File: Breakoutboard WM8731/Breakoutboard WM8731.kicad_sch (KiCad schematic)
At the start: 42 parts

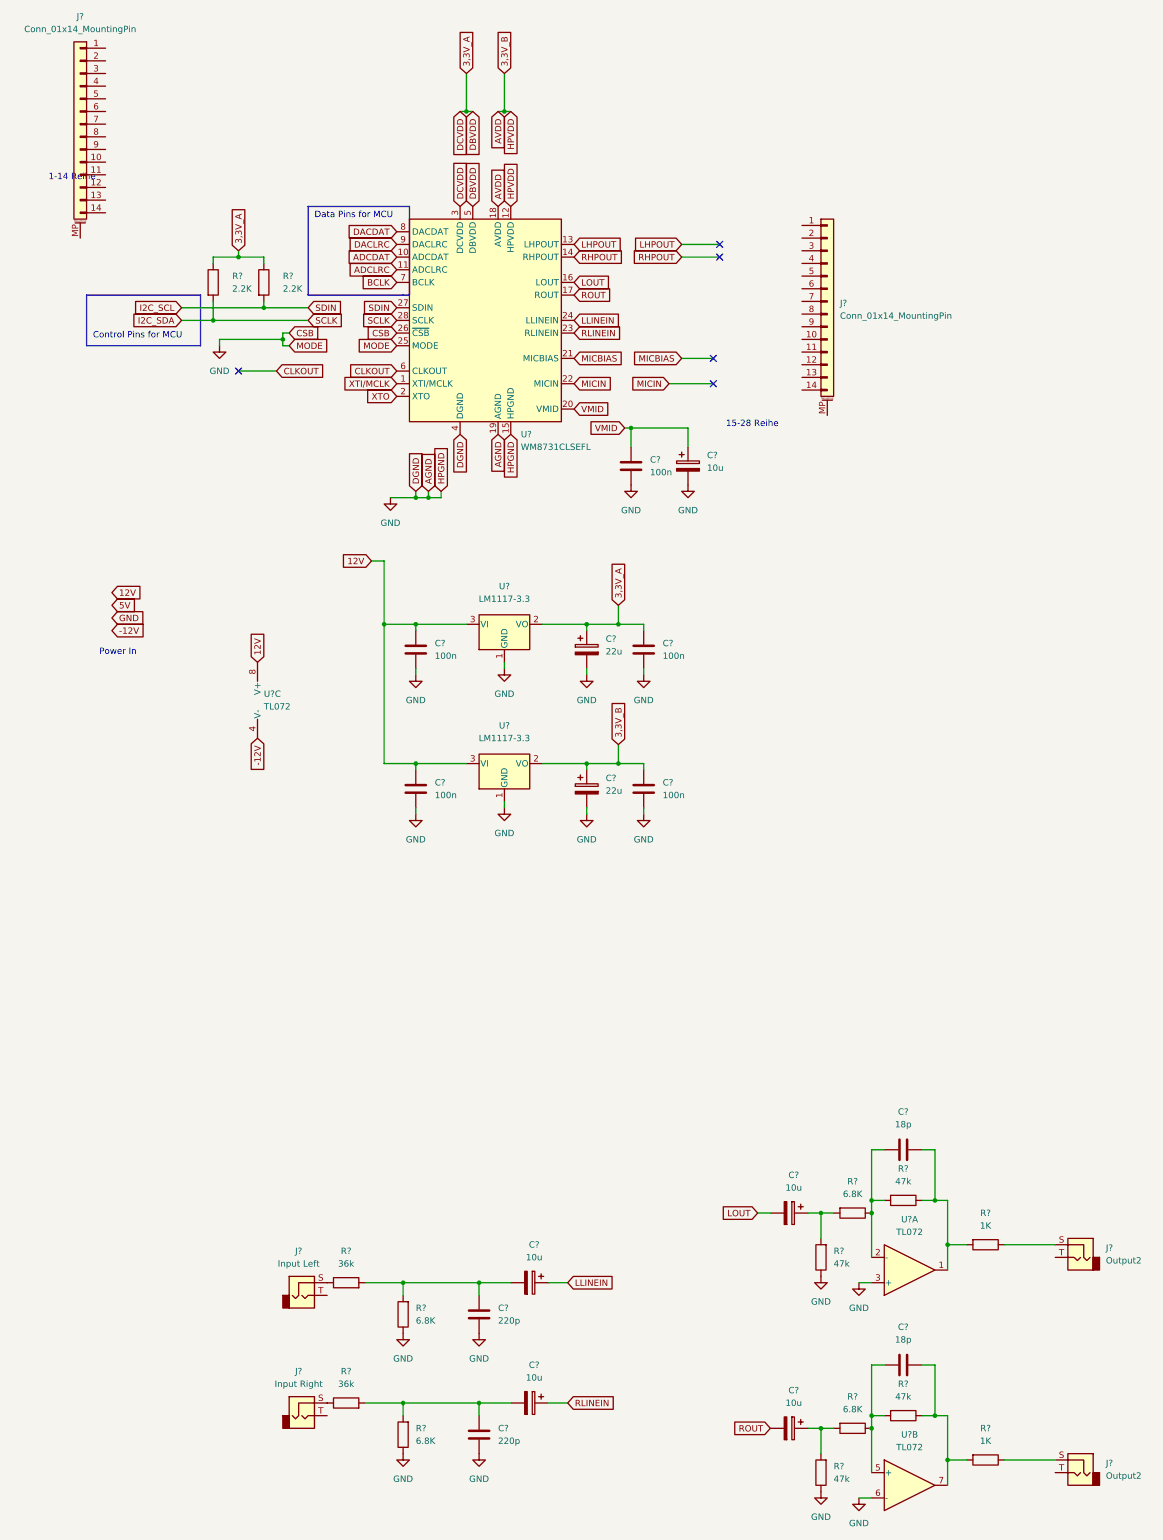
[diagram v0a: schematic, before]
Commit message: added esp sheet
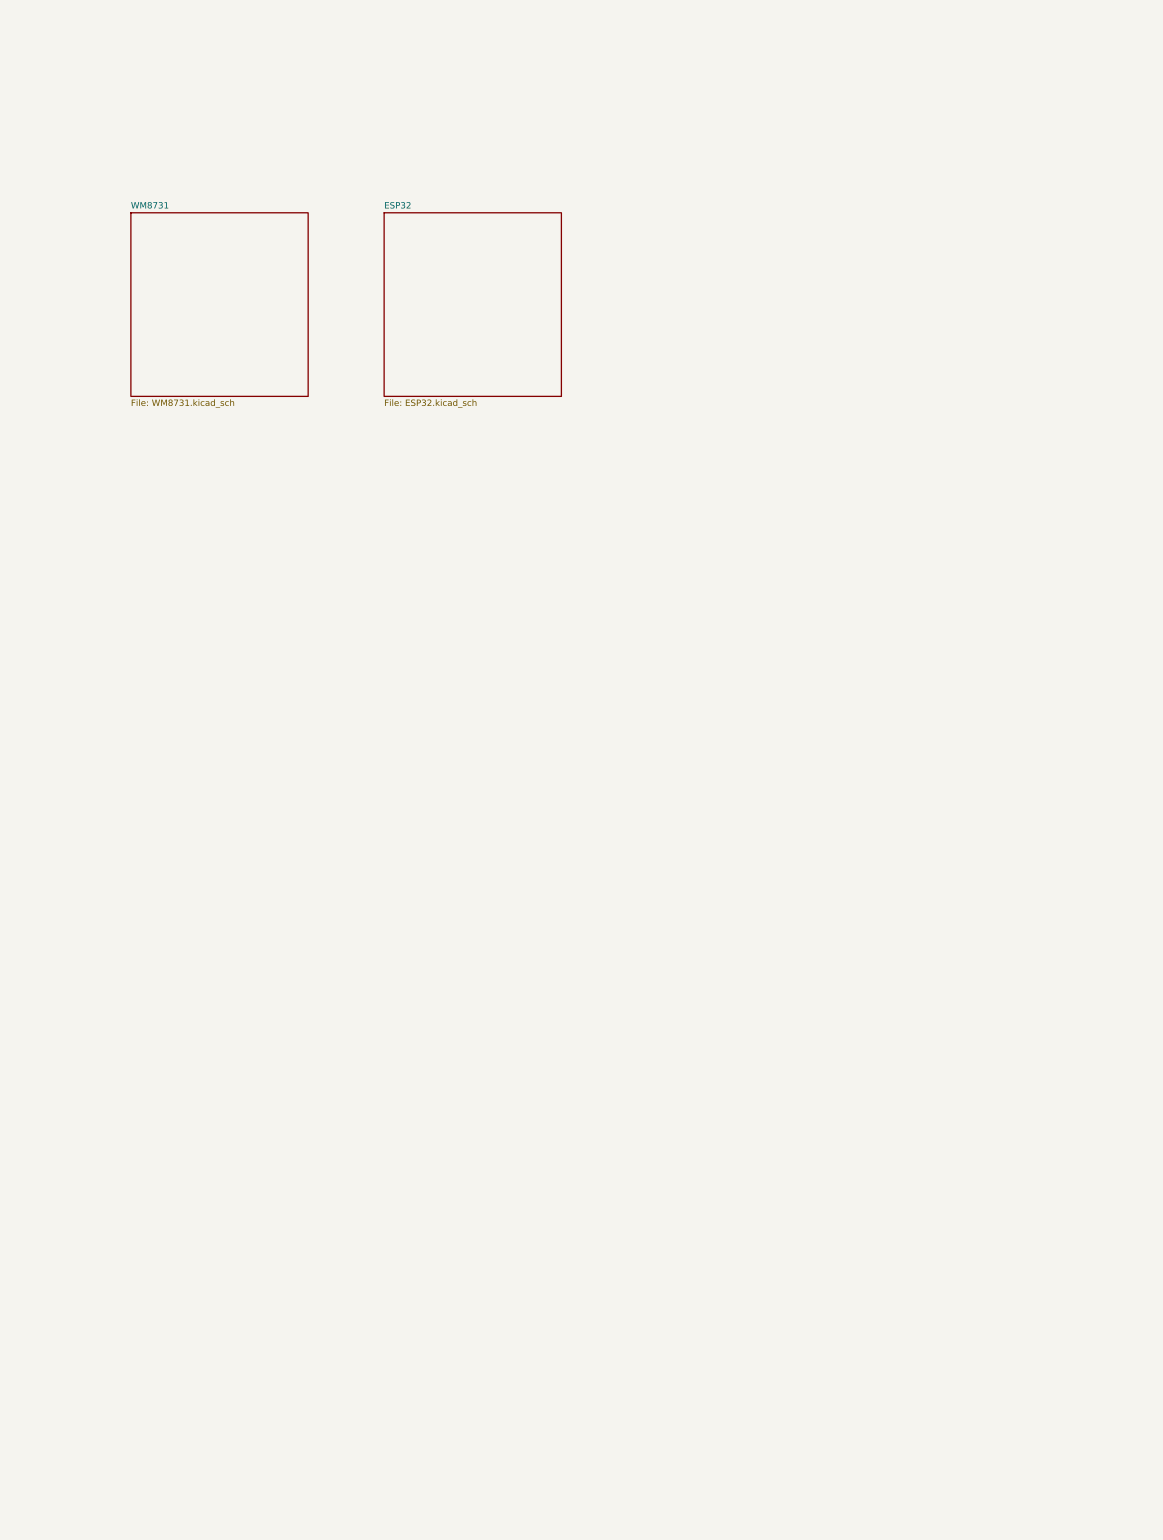
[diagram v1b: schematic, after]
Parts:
- removed C? (x2): 220p, symbol Device:C
- removed C? (x2): 22u, symbol Device:C_Polarized
- removed C? (x5): 10u, symbol Device:C_Polarized
- removed C? (x5): 100n, symbol Device:C
- removed C? (x2): 18p, symbol Device:C
- removed J? (x2): Output2, symbol Connector:AudioJack2
- removed J?: Input Left, symbol Connector:AudioJack2
- removed J? (x2): Conn_01x14_MountingPin, symbol Connector_Generic_MountingPin:Conn_01x14_MountingPin
- removed J?: Input Right, symbol Connector:AudioJack2
- removed R? (x2): 2.2K, symbol Device:R
- removed R? (x4): 6.8K, symbol Device:R
- removed R? (x4): 47k, symbol Device:R
- removed R? (x2): 36k, symbol Device:R
- removed R? (x2): 1K, symbol Device:R
- removed U? (x2): LM1117-3.3, symbol Regulator_Linear:LM1117-3.3
- removed U? (x3): TL072, symbol Amplifier_Operational:TL072
- removed U?: WM8731CLSEFL, Package_DFN_QFN:QFN-28-1EP_5x5mm_P0.5mm_EP3.35x3.35mm, symbol Audio:WM8731CLSEFL
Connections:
- no-connect marks 5 -> 0
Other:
- added sheet ESP32 (ESP32.kicad_sch)
- added sheet WM8731 (WM8731.kicad_sch)
- note removed: "1-14 Reihe"
- note removed: "15-28 Reihe"
- note removed: "Control Pins for MCU"
- note removed: "Data Pins for MCU"
- note removed: "Power In"
- title: (none) -> Breakoutboard WM8731
